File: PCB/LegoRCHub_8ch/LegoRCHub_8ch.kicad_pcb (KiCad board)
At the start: 2 copper layers, 39.3 x 55.2 mm, 42 parts, among them J1 Conn_01x02, J10 Conn_01x02, J2 Conn_01x02, J3 Conn_01x02, J4 Conn_01x02, J5 Conn_01x02, J6 Conn_01x03, J7 Conn_01x03, J8 Conn_01x03, J9 Conn_01x02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

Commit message: LegoRCHub_8ch: finished PCB (beta 4)
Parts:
- removed C13: 10uF, Capacitor_SMD:C_0603_1608Metric_Pad1.08x0.95mm_HandSolder
- removed C15: 470uF, Capacitor_SMD:CP_Elec_8x10.5
- removed R1, R2, R3, R4, R5: 10k, Resistor_SMD:R_0603_1608Metric_Pad0.98x0.95mm_HandSolder
- removed REF**: SOT-23-6, Package_TO_SOT_SMD:SOT-23-6
- added C16: 470uF, Capacitor_SMD:CP_Elec_8x10.5, B.Cu at (44.5, 71.8)
- added J11: Conn_01x03, Connector_JST:JST_XH_B3B-XH-A_1x03_P2.50mm_Vertical, B.Cu at (47.0, 61.2)
- J1, J2, J3, J4, J5: footprint Connector_PinHeader_2.54mm:PinHeader_1x02_P2.54mm_Vertical_SMD_Pin1Left -> Connector_PinHeader_2.54mm:PinHeader_1x02_P2.54mm_Vertical; moved to B.Cu
- J10: footprint Connector_PinHeader_2.54mm:PinHeader_1x02_P2.54mm_Vertical -> Connector_PinSocket_2.54mm:PinSocket_1x02_P2.54mm_Vertical; moved to B.Cu
- J6, J7, J8: footprint Connector_PinHeader_2.54mm:PinHeader_1x03_P2.54mm_Vertical_SMD_Pin1Left -> Connector_PinHeader_2.54mm:PinHeader_1x03_P2.54mm_Vertical; moved to B.Cu
- J9: moved to B.Cu
- moved J9 41.2 mm to (44.5, 32.3)
- moved U7 28.8 mm to (45.2, 53.3), turned to 180 degrees
- moved J6 26.4 mm to (60.5, 47.0), turned to 90 degrees
- moved C14 23.9 mm to (48.7, 46.7), turned to -90 degrees
- moved J7 22.8 mm to (60.5, 51.0), turned to 90 degrees
- moved C11 19.3 mm to (47.0, 42.8), turned to 90 degrees
- moved J8 18.0 mm to (60.5, 55.0), turned to 90 degrees
- moved J4 16.5 mm to (60.5, 38.1)
- moved U6 14.0 mm to (43.2, 44.8), turned to -90 degrees
- moved C9 12.7 mm to (57.5, 67.3), turned to 0 degrees
- moved U4 12.7 mm to (55.0, 37.3), turned to 0 degrees
- moved C12 12.3 mm to (47.0, 46.7), turned to -90 degrees
- moved J3 11.7 mm to (28.4, 64.0)
- moved J2 11.2 mm to (28.4, 51.5)
- moved J1 11.1 mm to (28.4, 39.5)
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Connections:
- J6 pad 3: /CH6_3 -> /CH6
- J7 pad 3: /CH7_3 -> /CH7
- J8 pad 3: /CH8_3 -> /CH8
- U1 pad 4: Net-(R1-Pad2) -> unconnected-(U1-Pad4)
- U2 pad 4: Net-(R2-Pad2) -> unconnected-(U2-Pad4)
- U3 pad 4: Net-(R3-Pad2) -> unconnected-(U3-Pad4)
- U4 pad 4: Net-(R4-Pad2) -> unconnected-(U4-Pad4)
- U5 pad 4: Net-(R5-Pad2) -> unconnected-(U5-Pad4)
- U7 pad 10: /CH6_3 -> /CH5_3
- U7 pad 11: /CH8_3 -> unconnected-(U7-Pad11)
- U7 pad 12: /CH7_3 -> unconnected-(U7-Pad12)
- U7 pad 13: unconnected-(U7-Pad13) -> /CH3_2
- U7 pad 14: /CH4_3 -> /CH3_3
- U7 pad 15: /CH4_2 -> /CH2_2
- U7 pad 17: /CH5_3 -> /CH2_3
- U7 pad 18: /CH5_2 -> /CH1_2
- U7 pad 19: unconnected-(U7-Pad19) -> /CH1_3
- U7 pad 2: /CH3_3 -> /CH4_3
- U7 pad 3: /CH3_2 -> /CH4_2
- U7 pad 4: /CH2_3 -> /CH6
- U7 pad 5: /CH2_2 -> /CH7
- U7 pad 6: /CH1_3 -> /CH8
- U7 pad 7: /CH1_2 -> unconnected-(U7-Pad7)
- U7 pad 8: unconnected-(U7-Pad8) -> /IBus
- U7 pad 9: unconnected-(U7-Pad9) -> /CH5_2
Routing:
- net VCC: track 111.1 -> 26.4 mm
- net /CH4_2: track 0.00 -> 19.0 mm, vias 0 -> 1
- net +BATT: track 0.00 -> 17.7 mm, vias 5 -> 25
- net /UPDI: track 0.00 -> 16.4 mm, vias 0 -> 1
- net /CH4_3: track 0.00 -> 16.2 mm, vias 0 -> 1
- net /CH1_3: track 0.00 -> 15.1 mm, vias 0 -> 1
- net /CH1_2: track 0.00 -> 14.6 mm, vias 0 -> 1
- net /CH3_2: track 0.00 -> 14.2 mm, vias 0 -> 1
- net /CH3_3: track 0.00 -> 13.7 mm, vias 0 -> 1
- net /CH6: track 0.00 -> 9.47 mm
- net /CH5_2: track 0.00 -> 8.49 mm, vias 0 -> 1
- net /CH5_3: track 0.00 -> 8.48 mm, vias 0 -> 1
- net /IBus: track 0.00 -> 7.96 mm
- net GND: track 0.00 -> 7.95 mm
- net /CH7: track 0.00 -> 7.49 mm
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- added copper zone on B.Cu, net VCC

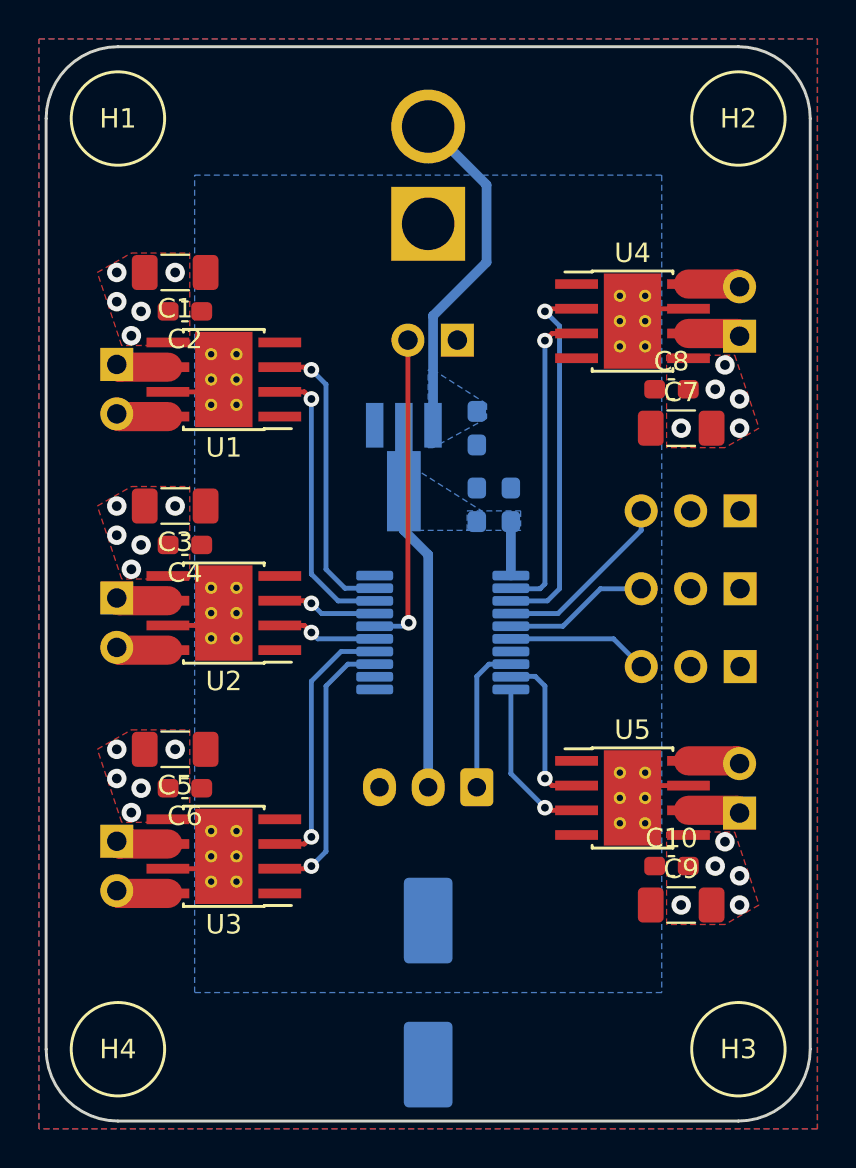
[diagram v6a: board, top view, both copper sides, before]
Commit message: LegoRCHub_8ch: finished PCB (beta 5)
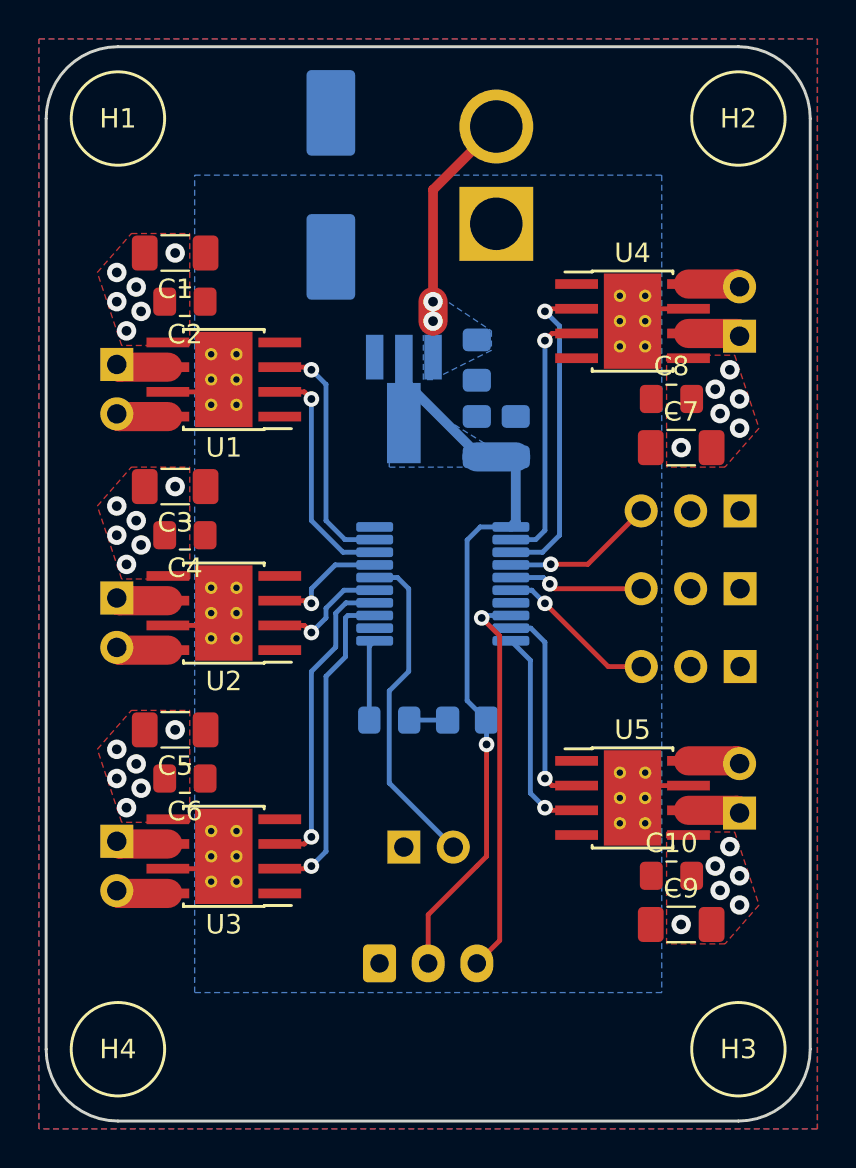
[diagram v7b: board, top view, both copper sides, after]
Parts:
- removed C16: 470uF, Capacitor_SMD:CP_Elec_8x10.5
- added C15: 470uF, Capacitor_SMD:CP_Elec_8x10.5, B.Cu at (39.5, 30.3)
- added D1: Blue, LED_SMD:LED_0805_2012Metric_Pad1.15x1.40mm_HandSolder, B.Cu at (42.5, 57.8)
- added R1: 4.7k, Resistor_SMD:R_0805_2012Metric_Pad1.20x1.40mm_HandSolder, B.Cu at (46.5, 57.8)
- C10, C11, C14, C2, C4, C6, C8: footprint Capacitor_SMD:C_0603_1608Metric_Pad1.08x0.95mm_HandSolder -> Capacitor_SMD:C_0805_2012Metric_Pad1.18x1.45mm_HandSolder
- C12: value 22uF -> 47uF; footprint Capacitor_SMD:C_0603_1608Metric_Pad1.08x0.95mm_HandSolder -> Capacitor_SMD:C_0805_2012Metric_Pad1.18x1.45mm_HandSolder
- moved J10 26.2 mm to (43.2, 64.3), turned to -90 degrees
- moved J11 10.3 mm to (42.0, 70.3), turned to 0 degrees
- moved C14 3.51 mm to (49.0, 43.2)
- moved C11 3.50 mm to (47.0, 39.3)
- moved C12 3.50 mm to (47.0, 43.2)
- moved J9 3.50 mm to (48.0, 32.3)
- moved U6 3.50 mm to (43.2, 41.3)
- moved U7 2.50 mm to (45.2, 50.8)
- moved C1 1.00 mm to (31.4, 33.8)
- moved C3 1.00 mm to (31.4, 45.8)
- moved C5 1.00 mm to (31.4, 58.3)
- moved C7 1.00 mm to (57.5, 43.8)
- moved C9 1.00 mm to (57.5, 68.3)
- moved C10 0.50 mm to (57.0, 65.8)
- moved C2 0.50 mm to (31.9, 36.3)
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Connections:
- J11 pad 1: /IBus -> GND
- J11 pad 3: GND -> /IBus
- U7 pad 11: unconnected-(U7-Pad11) -> Net-(U7-Pad11)
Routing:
- net /IBus: track 7.96 -> 20.2 mm, vias 0 -> 1
- net VCC: track 26.4 -> 38.1 mm, vias 0 -> 1
- net +BATT: track 17.7 -> 11.3 mm, vias 25 -> 32
- net Net-(U7-Pad11): track 0.00 -> 4.19 mm
- net /CH4_3: track 16.2 -> 13.5 mm
- net /CH4_2: track 19.0 -> 16.4 mm
- net /CH1_2: track 14.6 -> 11.9 mm
- net /CH5_3: track 8.48 -> 11.0 mm
- net /CH3_2: track 14.2 -> 16.7 mm
- net /CH1_3: track 15.1 -> 12.6 mm
- net /CH3_3: track 13.7 -> 16.0 mm
- net /CH5_2: track 8.49 -> 10.8 mm
- net Net-(D1-Pad1): track 0.00 -> 1.98 mm
- net /CH6: track 9.47 -> 7.84 mm, vias 0 -> 1
- net /CH2_2: track 5.16 -> 6.22 mm
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
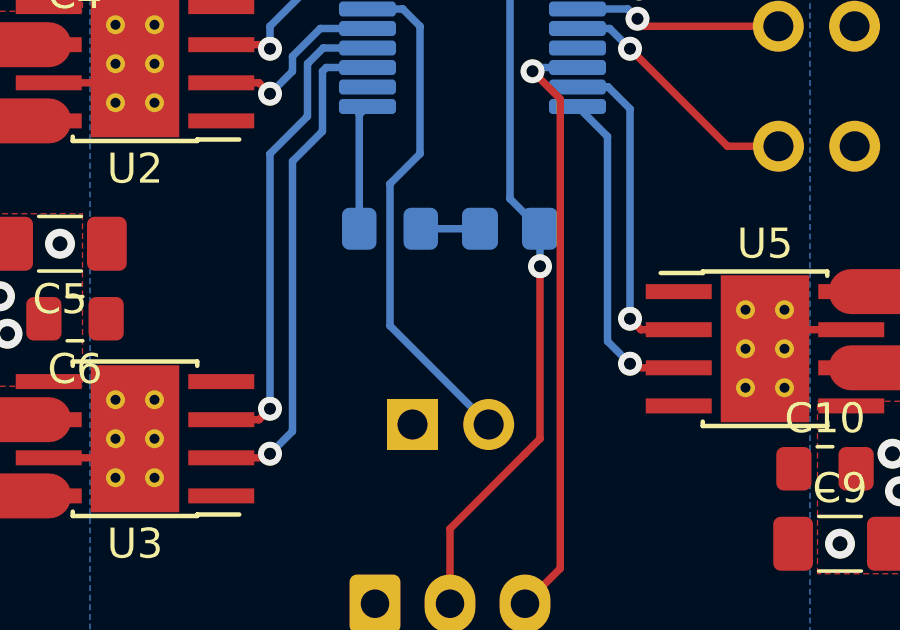
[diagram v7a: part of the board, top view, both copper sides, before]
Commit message: LegoRCHub_8ch: finished PCB (beta 6)
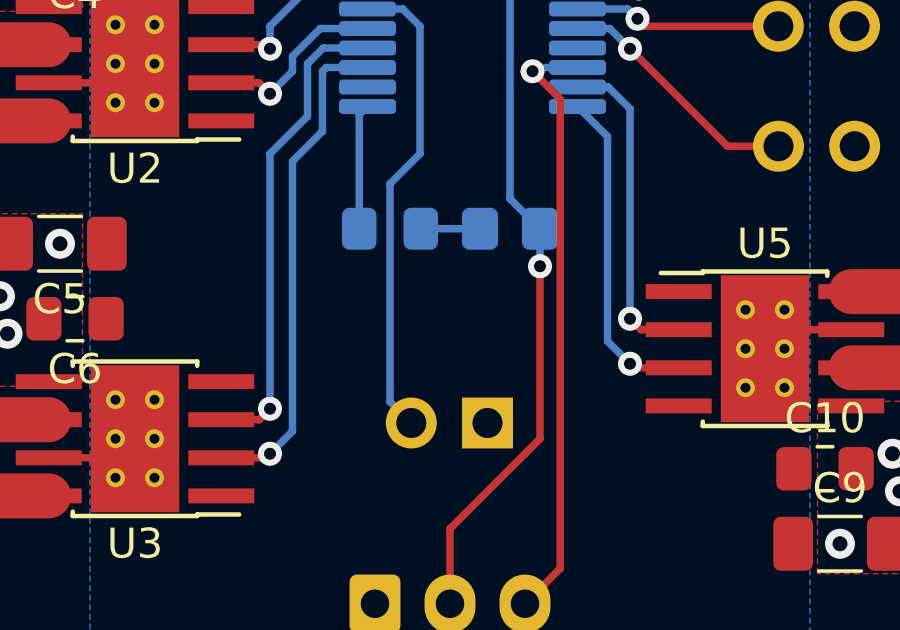
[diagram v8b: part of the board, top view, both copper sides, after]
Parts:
- moved J10 2.50 mm to (45.7, 64.3), turned to 90 degrees
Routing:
- net /UPDI: track 17.0 -> 15.9 mm
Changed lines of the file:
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@@
   )
   (footprint "Connector_PinSocket_2.54mm:PinSocket_1x02_P2.54mm_Vertical" (layer "B.Cu")
-    (at 43.2 64.325 -90)
+    (at 45.7 64.275 90)
     (descr "Through hole straight socket strip, 1x02, 2.54mm pitch, single row (from Kicad 4.0.7), script generated")
     (tags "Through hole socket strip THT 1x02 2.54mm single row")
@@
     (fp_line (start -1.27 -3.81) (end -1.27 1.27) (layer "B.Fab") (width 0.1))
     (fp_line (start 1.27 -3.81) (end -1.27 -3.81) (layer "B.Fab") (width 0.1))
-    (pad "1" thru_hole rect (at 0 0 270) (size 1.7 1.7) (drill 1) (layers *.Cu *.Mask)
+    (pad "1" thru_hole rect (at 0 0 90) (size 1.7 1.7) (drill 1) (layers *.Cu *.Mask)
       (net 1 "GND") (pinfunction "Pin_1") (pintype "passive"))
-    (pad "2" thru_hole oval (at 0 -2.54 270) (size 1.7 1.7) (drill 1) (layers *.Cu *.Mask)
+    (pad "2" thru_hole oval (at 0 -2.54 90) (size 1.7 1.7) (drill 1) (layers *.Cu *.Mask)
       (net 24 "/UPDI") (pinfunction "Pin_2") (pintype "passive"))
     (model "${KICAD6_3DMODEL_DIR}/Connector_PinSocket_2.54mm.3dshapes/PinSocket_1x02_P2.54mm_Vertical.wrl"
@@
   (segment (start 49.7 54.725) (end 48.7 53.725) (width 0.25) (layer "B.Cu") (net 23))
   (segment (start 50.45 62.3) (end 49.7 61.55) (width 0.25) (layer "B.Cu") (net 23))
+  (segment (start 42.45 63.565) (end 43.16 64.275) (width 0.25) (layer "B.Cu") (net 24))
+  (segment (start 41.7 50.475) (end 42.875 50.475) (width 0.25) (layer "B.Cu") (net 24))
+  (segment (start 42.45 56.3) (end 42.45 63.565) (width 0.25) (layer "B.Cu") (net 24))
+  (segment (start 43.45 55.3) (end 42.45 56.3) (width 0.25) (layer "B.Cu") (net 24))
   (segment (start 42.875 50.475) (end 43.45 51.05) (width 0.25) (layer "B.Cu") (net 24))
-  (segment (start 42.45 61.035) (end 45.74 64.325) (width 0.25) (layer "B.Cu") (net 24))
-  (segment (start 41.7 50.475) (end 42.875 50.475) (width 0.25) (layer "B.Cu") (net 24))
-  (segment (start 43.45 55.3) (end 42.45 56.3) (width 0.25) (layer "B.Cu") (net 24))
   (segment (start 43.45 51.05) (end 43.45 55.3) (width 0.25) (layer "B.Cu") (net 24))
-  (segment (start 42.45 56.3) (end 42.45 61.035) (width 0.25) (layer "B.Cu") (net 24))
   (segment (start 53.7 55.05) (end 55.399999 55.05) (width 0.25) (layer "F.Cu") (net 25))
   (segment (start 50.45 51.8) (end 53.7 55.05) (width 0.25) (layer "F.Cu") (net 25))
